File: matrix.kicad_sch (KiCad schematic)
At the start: 138 parts, among them SW1 SW_Push, SW10 SW_Push, SW11 SW_Push, SW12 SW_Push, SW13 SW_Push, SW14 SW_Push, SW15 SW_Push, SW16 SW_Push, SW17 SW_Push, SW18 SW_Push, SW19 SW_Push, SW2 SW_Push, SW20 SW_Push, SW21 SW_Push, SW22 SW_Push, SW23 SW_Push, SW24 SW_Push, SW25 SW_Push, SW26 SW_Push, SW27 SW_Push, SW28 SW_Push, SW29 SW_Push, SW3 SW_Push, SW30 SW_Push, SW31 SW_Push, SW32 SW_Push, SW33 SW_Push, SW34 SW_Push, SW35 SW_Push, SW36 SW_Push, SW37 SW_Push, SW38 SW_Push, SW39 SW_Push, SW4 SW_Push, SW40 SW_Push, SW41 SW_Push, SW42 SW_Push, SW43 SW_Push, SW44 SW_Push, SW45 SW_Push, SW46 SW_Push, SW47 SW_Push, SW48 SW_Push, SW49 SW_Push, SW5 SW_Push, SW50 SW_Push, SW51 SW_Push, SW52 SW_Push, SW53 SW_Push, SW54 SW_Push, SW55 SW_Push, SW56 SW_Push, SW57 SW_Push, SW58 SW_Push, SW59 SW_Push, SW6 SW_Push, SW60 SW_Push, SW61 SW_Push, SW62 SW_Push, SW63 SW_Push, SW65 SW_Push, SW66 SW_Push, SW67 SW_Push, SW69 SW_Push, SW7 SW_Push, SW70 SW_Push, SW71 SW_Push, SW8 SW_Push, SW9 SW_Push

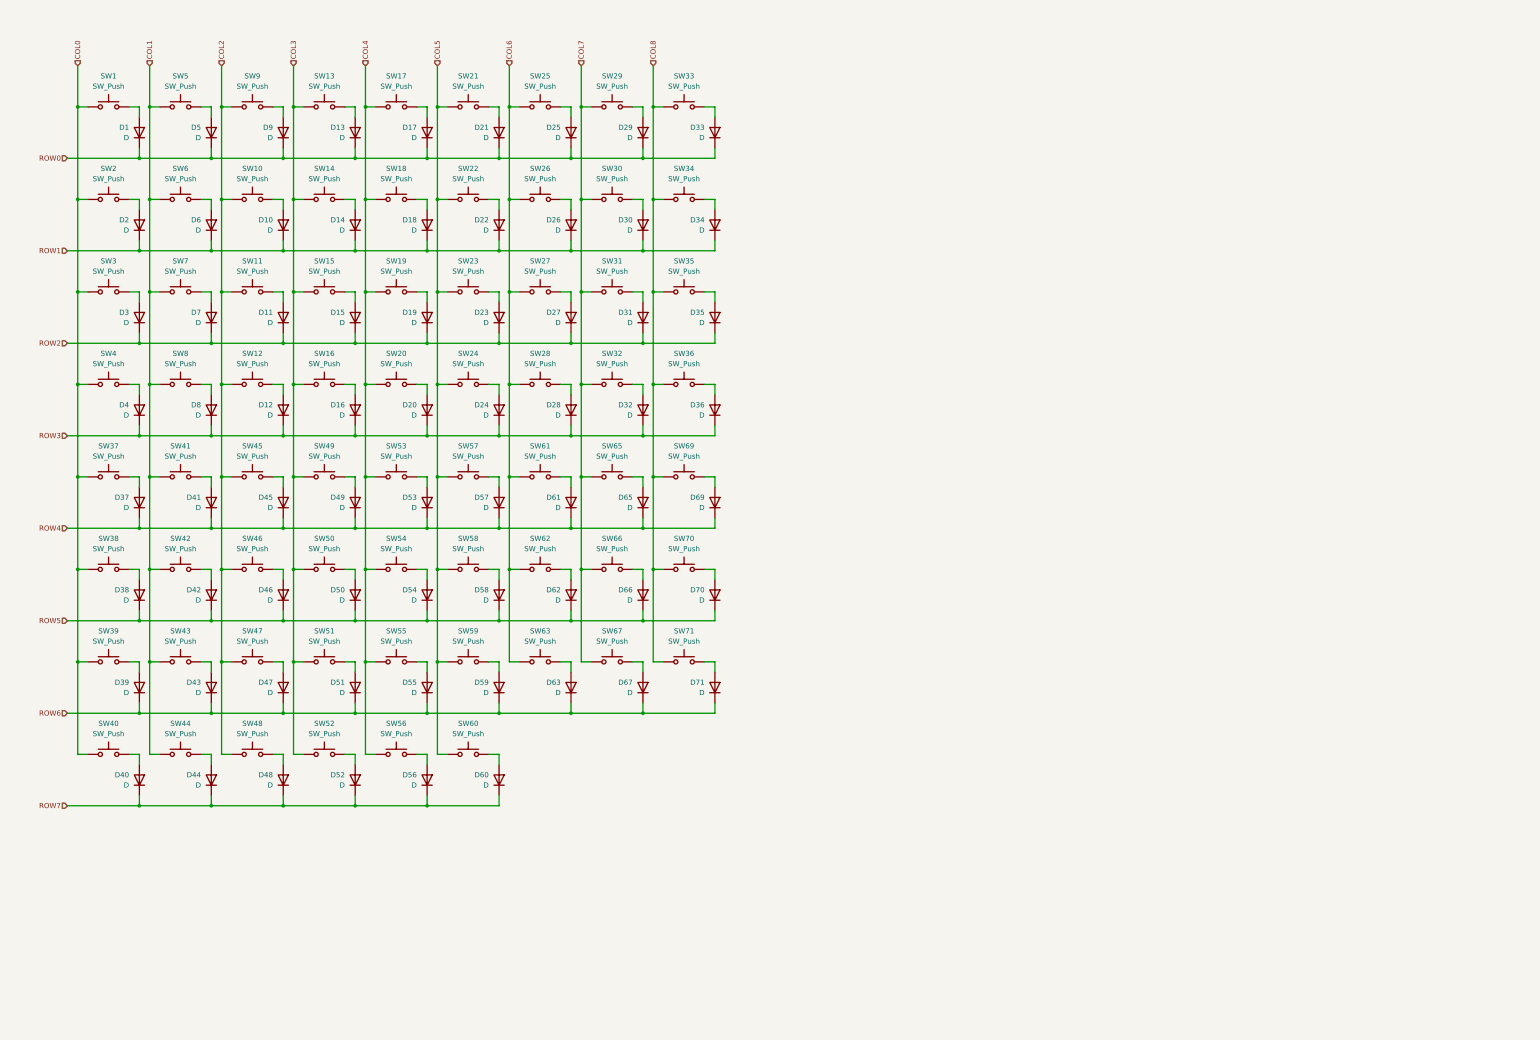
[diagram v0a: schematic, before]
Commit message: update layout and switch to wired
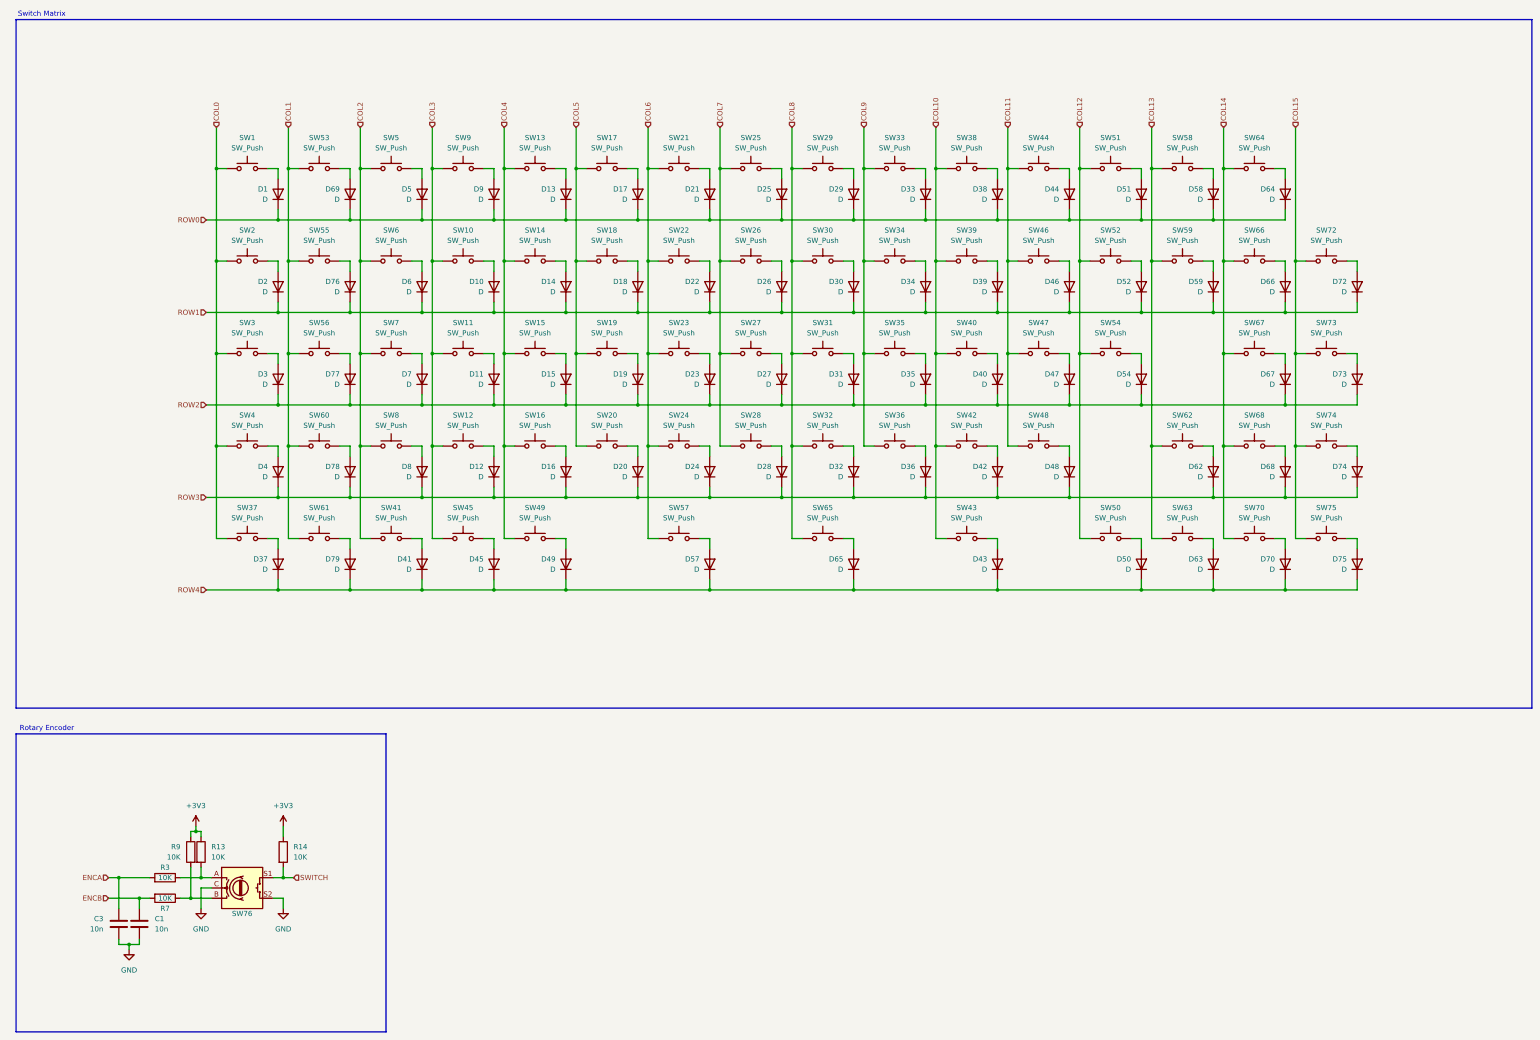
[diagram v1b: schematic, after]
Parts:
- removed D53, D55, D56, D60, D61, D71: D, symbol Device:D
- removed SW69, SW71: SW_Push, symbol Switch:SW_Push
- added C1, C3: 10n, symbol Device:C
- added D64, D68, D72, D73, D74, D75, D76, D77, D78, D79: D, symbol Device:D
- added R13, R14, R3, R7, R9: 10K, symbol Device:R
- added SW64, SW68, SW72, SW73, SW74, SW75: SW_Push, symbol Switch:SW_Push
- added SW76: RotaryEncoder_Switch, symbol Device:RotaryEncoder_Switch
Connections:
- net COL0: no longer SW38.1, SW39.1, SW40.1
- net COL1: now also SW53.1, SW55.1, SW56.1, SW60.1, SW61.1; no longer SW41.1, SW42.1, SW43.1, SW44.1, SW5.1, SW6.1, SW7.1, SW8.1
- net COL2: now also SW41.1, SW5.1, SW6.1, SW7.1, SW8.1; no longer SW10.1, SW11.1, SW12.1, SW45.1, SW46.1, SW47.1, SW48.1, SW9.1
- net COL3: now also SW10.1, SW11.1, SW12.1, SW45.1, SW9.1; no longer SW13.1, SW14.1, SW15.1, SW16.1, SW49.1, SW50.1, SW51.1, SW52.1
- net COL4: now also SW13.1, SW14.1, SW15.1, SW16.1, SW49.1; no longer SW17.1, SW18.1, SW19.1, SW20.1, SW53.1, SW54.1, SW55.1, SW56.1
- net COL5: now also SW17.1, SW18.1, SW19.1, SW20.1; no longer SW21.1, SW22.1, SW23.1, SW24.1, SW57.1, SW58.1, SW59.1, SW60.1
- net COL6: now also SW21.1, SW22.1, SW23.1, SW24.1, SW57.1; no longer SW25.1, SW26.1, SW27.1, SW28.1, SW61.1, SW62.1, SW63.1
- net COL7: now also SW25.1, SW26.1, SW27.1, SW28.1; no longer SW29.1, SW30.1, SW31.1, SW32.1, SW65.1, SW66.1, SW67.1
- net COL8: now also SW29.1, SW30.1, SW31.1, SW32.1, SW65.1; no longer SW33.1, SW34.1, SW35.1, SW36.1, SW70.1
- net ROW0: now also D38.1 (K), D44.1 (K), D51.1 (K), D58.1 (K), D69.1 (K), D64.1 (K)
- net ROW1: now also D39.1 (K), D46.1 (K), D52.1 (K), D59.1 (K), D66.1 (K), D72.1 (K), D76.1 (K)
- net ROW2: now also D40.1 (K), D47.1 (K), D54.1 (K), D67.1 (K), D73.1 (K), D77.1 (K)
- net ROW3: now also D42.1 (K), D48.1 (K), D62.1 (K), D68.1 (K), D74.1 (K), D78.1 (K)
- net ROW4: now also D43.1 (K), D50.1 (K), D63.1 (K), D70.1 (K), D75.1 (K), D79.1 (K); no longer D69.1 (K)
- net at SW55.2: now also D76.2 (A)
- net at SW60.2: now also D78.2 (A)
- net at SW61.2: now also D79.2 (A)
- net at SW56.2: now also D77.2 (A)
- net at SW53.2: now also D69.2 (A)
- removed net ROW5: D38.1 (K), D42.1 (K), D46.1 (K), D50.1 (K), D54.1 (K), D58.1 (K), D62.1 (K), D66.1 (K), D70.1 (K)
- removed net ROW6: D39.1 (K), D43.1 (K), D47.1 (K), D51.1 (K), D59.1 (K), D63.1 (K), D67.1 (K)
- removed net ROW7: D40.1 (K), D44.1 (K), D48.1 (K), D52.1 (K)
- new net: D74.2 (A), SW74.2
- new net: R13.2, R3.1, SW76.A
- new net: D75.2 (A), SW75.2
- new net: D68.2 (A), SW68.2
- new net: D72.2 (A), SW72.2
- new net: D73.2 (A), SW73.2
- new net: R7.1, R9.2, SW76.B
- new net: D64.2 (A), SW64.2
- new net +3V3: R13.1, R14.1, R9.1
- new net COL10: SW38.1, SW39.1, SW40.1, SW42.1, SW43.1
- new net COL11: SW44.1, SW46.1, SW47.1, SW48.1
- new net COL12: SW50.1, SW51.1, SW52.1, SW54.1
- new net COL13: SW58.1, SW59.1, SW62.1, SW63.1
- new net COL14: SW64.1, SW66.1, SW67.1, SW68.1, SW70.1
- new net COL15: SW72.1, SW73.1, SW74.1, SW75.1
- new net COL9: SW33.1, SW34.1, SW35.1, SW36.1
- new net ENCA: C3.1, R3.2
- new net ENCB: C1.1, R7.2
- new net GND: C1.2, C3.2, SW76.C, SW76.S2
- new net SWITCH: R14.2, SW76.S1
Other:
- note added: "Rotary Encoder"
- note added: "Switch Matrix"
- moved on the sheet: D10, D11, D12, D13, D14, D15, D16, D17, D18, D19, D20, D21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

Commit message: work on layout and routing
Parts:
- C14: renamed from C3; footprint (none) -> Capacitor_SMD:C_0402_1005Metric
- C15: renamed from C1; footprint (none) -> Capacitor_SMD:C_0402_1005Metric
- D1, D22: footprint (none) -> Diode_SMD:D_SOD-123
- D10: renamed from D33; footprint (none) -> Diode_SMD:D_SOD-123
- D11: renamed from D38; footprint (none) -> Diode_SMD:D_SOD-123
- D12: renamed from D44; footprint (none) -> Diode_SMD:D_SOD-123
- D13: renamed from D51; footprint (none) -> Diode_SMD:D_SOD-123
- D14: renamed from D58; footprint (none) -> Diode_SMD:D_SOD-123
- D15: renamed from D64; footprint (none) -> Diode_SMD:D_SOD-123
- D16: renamed from D2; footprint (none) -> Diode_SMD:D_SOD-123
- D17: renamed from D76; footprint (none) -> Diode_SMD:D_SOD-123
- D18: renamed from D6; footprint (none) -> Diode_SMD:D_SOD-123
- D19: renamed from D10; footprint (none) -> Diode_SMD:D_SOD-123
- D2: renamed from D69; footprint (none) -> Diode_SMD:D_SOD-123
- D20: renamed from D14; footprint (none) -> Diode_SMD:D_SOD-123
- D21: renamed from D18; footprint (none) -> Diode_SMD:D_SOD-123
- D23: renamed from D26; footprint (none) -> Diode_SMD:D_SOD-123
- D24: renamed from D30; footprint (none) -> Diode_SMD:D_SOD-123
- D25: renamed from D34; footprint (none) -> Diode_SMD:D_SOD-123
- D26: renamed from D39; footprint (none) -> Diode_SMD:D_SOD-123
- D27: renamed from D46; footprint (none) -> Diode_SMD:D_SOD-123
- D28: renamed from D52; footprint (none) -> Diode_SMD:D_SOD-123
- D29: renamed from D59; footprint (none) -> Diode_SMD:D_SOD-123
- D3: renamed from D5; footprint (none) -> Diode_SMD:D_SOD-123
- D30: renamed from D66; footprint (none) -> Diode_SMD:D_SOD-123
- D31: renamed from D72; footprint (none) -> Diode_SMD:D_SOD-123
- D32: renamed from D3; footprint (none) -> Diode_SMD:D_SOD-123
- D33: renamed from D77; footprint (none) -> Diode_SMD:D_SOD-123
- D34: renamed from D7; footprint (none) -> Diode_SMD:D_SOD-123
- D35: renamed from D11; footprint (none) -> Diode_SMD:D_SOD-123
- D36: renamed from D15; footprint (none) -> Diode_SMD:D_SOD-123
- D37: renamed from D19; footprint (none) -> Diode_SMD:D_SOD-123
- D38: renamed from D23; footprint (none) -> Diode_SMD:D_SOD-123
- D39: renamed from D27; footprint (none) -> Diode_SMD:D_SOD-123
- D4: renamed from D9; footprint (none) -> Diode_SMD:D_SOD-123
- D40: renamed from D31; footprint (none) -> Diode_SMD:D_SOD-123
- D41: renamed from D35; footprint (none) -> Diode_SMD:D_SOD-123
- D42: renamed from D40; footprint (none) -> Diode_SMD:D_SOD-123
- D43: renamed from D47; footprint (none) -> Diode_SMD:D_SOD-123
- D44: renamed from D54; footprint (none) -> Diode_SMD:D_SOD-123
- D45: renamed from D67; footprint (none) -> Diode_SMD:D_SOD-123
- D46: renamed from D73; footprint (none) -> Diode_SMD:D_SOD-123
- D47: renamed from D4; footprint (none) -> Diode_SMD:D_SOD-123
- D48: renamed from D78; footprint (none) -> Diode_SMD:D_SOD-123
- D49: renamed from D8; footprint (none) -> Diode_SMD:D_SOD-123
- D5: renamed from D13; footprint (none) -> Diode_SMD:D_SOD-123
- D50: renamed from D12; footprint (none) -> Diode_SMD:D_SOD-123
- D51: renamed from D16; footprint (none) -> Diode_SMD:D_SOD-123
- D52: renamed from D20; footprint (none) -> Diode_SMD:D_SOD-123
- D53: renamed from D24; footprint (none) -> Diode_SMD:D_SOD-123
- D54: renamed from D28; footprint (none) -> Diode_SMD:D_SOD-123
- D55: renamed from D32; footprint (none) -> Diode_SMD:D_SOD-123
- D56: renamed from D36; footprint (none) -> Diode_SMD:D_SOD-123
- D57: renamed from D42; footprint (none) -> Diode_SMD:D_SOD-123
- D58: renamed from D48; footprint (none) -> Diode_SMD:D_SOD-123
- D59: renamed from D62; footprint (none) -> Diode_SMD:D_SOD-123
- D6: renamed from D17; footprint (none) -> Diode_SMD:D_SOD-123
- D60: renamed from D68; footprint (none) -> Diode_SMD:D_SOD-123
- D61: renamed from D74; footprint (none) -> Diode_SMD:D_SOD-123
- D62: renamed from D37; footprint (none) -> Diode_SMD:D_SOD-123
- D63: renamed from D79; footprint (none) -> Diode_SMD:D_SOD-123
- D64: renamed from D41; footprint (none) -> Diode_SMD:D_SOD-123
- D65: renamed from D45; footprint (none) -> Diode_SMD:D_SOD-123
- D66: renamed from D49; footprint (none) -> Diode_SMD:D_SOD-123
- D67: renamed from D57; footprint (none) -> Diode_SMD:D_SOD-123
- D68: renamed from D65; footprint (none) -> Diode_SMD:D_SOD-123
- D69: renamed from D43; footprint (none) -> Diode_SMD:D_SOD-123
- D7: renamed from D21; footprint (none) -> Diode_SMD:D_SOD-123
- D70: renamed from D50; footprint (none) -> Diode_SMD:D_SOD-123
- D71: renamed from D63; footprint (none) -> Diode_SMD:D_SOD-123
- D72: renamed from D70; footprint (none) -> Diode_SMD:D_SOD-123
- D73: renamed from D75; footprint (none) -> Diode_SMD:D_SOD-123
- D8: renamed from D25; footprint (none) -> Diode_SMD:D_SOD-123
- D9: renamed from D29; footprint (none) -> Diode_SMD:D_SOD-123
- R12: renamed from R9; footprint (none) -> Resistor_SMD:R_0402_1005Metric
- R13, R14: footprint (none) -> Resistor_SMD:R_0402_1005Metric
- R15: renamed from R3; footprint (none) -> Resistor_SMD:R_0402_1005Metric
- R16: renamed from R7; footprint (none) -> Resistor_SMD:R_0402_1005Metric
- SW1, SW22: footprint (none) -> PCM_marbastlib-mx:SW_MX_1u
- SW10: renamed from SW33; footprint (none) -> PCM_marbastlib-mx:SW_MX_1u
- SW11: renamed from SW38; footprint (none) -> PCM_marbastlib-mx:SW_MX_1u
- SW12: renamed from SW44; footprint (none) -> PCM_marbastlib-mx:SW_MX_1u
- SW13: renamed from SW51; footprint (none) -> PCM_marbastlib-mx:SW_MX_1u
- SW14: renamed from SW58; footprint (none) -> PCM_marbastlib-mx:SW_MX_1u
- SW15: renamed from SW64; footprint (none) -> PCM_marbastlib-mx:SW_MX_1u
- SW16: renamed from SW2; footprint (none) -> PCM_marbastlib-mx:SW_MX_1u
- SW17: renamed from SW55; footprint (none) -> PCM_marbastlib-mx:SW_MX_1u
- SW18: renamed from SW6; footprint (none) -> PCM_marbastlib-mx:SW_MX_1u
- SW19: renamed from SW10; footprint (none) -> PCM_marbastlib-mx:SW_MX_1u
- SW2: renamed from SW53; footprint (none) -> PCM_marbastlib-mx:SW_MX_1u
- SW20: renamed from SW14; footprint (none) -> PCM_marbastlib-mx:SW_MX_1u
- SW21: renamed from SW18; footprint (none) -> PCM_marbastlib-mx:SW_MX_1u
- SW23: renamed from SW26; footprint (none) -> PCM_marbastlib-mx:SW_MX_1u
- SW24: renamed from SW30; footprint (none) -> PCM_marbastlib-mx:SW_MX_1u
- SW25: renamed from SW34; footprint (none) -> PCM_marbastlib-mx:SW_MX_1u
- SW26: renamed from SW39; footprint (none) -> PCM_marbastlib-mx:SW_MX_1u
- SW27: renamed from SW46; footprint (none) -> PCM_marbastlib-mx:SW_MX_1u
- SW28: renamed from SW52; footprint (none) -> PCM_marbastlib-mx:SW_MX_1u
- SW29: renamed from SW59; footprint (none) -> PCM_marbastlib-mx:SW_MX_1u
- SW3: renamed from SW5; footprint (none) -> PCM_marbastlib-mx:SW_MX_1u
- SW30: renamed from SW66; footprint (none) -> PCM_marbastlib-mx:SW_MX_1u
- SW31: renamed from SW72; footprint (none) -> PCM_marbastlib-mx:SW_MX_1u
- SW32: renamed from SW3; footprint (none) -> PCM_marbastlib-mx:SW_MX_1u
- SW33: renamed from SW56; footprint (none) -> PCM_marbastlib-mx:SW_MX_1u
- SW34: renamed from SW7; footprint (none) -> PCM_marbastlib-mx:SW_MX_1u
- SW35: renamed from SW11; footprint (none) -> PCM_marbastlib-mx:SW_MX_1u
- SW36: renamed from SW15; footprint (none) -> PCM_marbastlib-mx:SW_MX_1u
- SW37: renamed from SW19; footprint (none) -> PCM_marbastlib-mx:SW_MX_1u
- SW38: renamed from SW23; footprint (none) -> PCM_marbastlib-mx:SW_MX_1u
- SW39: renamed from SW27; footprint (none) -> PCM_marbastlib-mx:SW_MX_1u
- SW4: renamed from SW9; footprint (none) -> PCM_marbastlib-mx:SW_MX_1u
- SW40: renamed from SW31; footprint (none) -> PCM_marbastlib-mx:SW_MX_1u
- SW41: renamed from SW35; footprint (none) -> PCM_marbastlib-mx:SW_MX_1u
- SW42: renamed from SW40; footprint (none) -> PCM_marbastlib-mx:SW_MX_1u
- SW43: renamed from SW47; footprint (none) -> PCM_marbastlib-mx:SW_MX_1u
- SW44: renamed from SW54; footprint (none) -> PCM_marbastlib-mx:SW_MX_1u
- SW45: renamed from SW67; footprint (none) -> PCM_marbastlib-mx:SW_MX_1u
- SW46: renamed from SW73; footprint (none) -> PCM_marbastlib-mx:SW_MX_1u
- SW47: renamed from SW4; footprint (none) -> PCM_marbastlib-mx:SW_MX_1u
- SW48: renamed from SW60; footprint (none) -> PCM_marbastlib-mx:SW_MX_1u
- SW49: renamed from SW8; footprint (none) -> PCM_marbastlib-mx:SW_MX_1u
- SW5: renamed from SW13; footprint (none) -> PCM_marbastlib-mx:SW_MX_1u
- SW50: renamed from SW12; footprint (none) -> PCM_marbastlib-mx:SW_MX_1u
- SW51: renamed from SW16; footprint (none) -> PCM_marbastlib-mx:SW_MX_1u
- SW52: renamed from SW20; footprint (none) -> PCM_marbastlib-mx:SW_MX_1u
- SW53: renamed from SW24; footprint (none) -> PCM_marbastlib-mx:SW_MX_1u
- SW54: renamed from SW28; footprint (none) -> PCM_marbastlib-mx:SW_MX_1u
- SW55: renamed from SW32; footprint (none) -> PCM_marbastlib-mx:SW_MX_1u
- SW56: renamed from SW36; footprint (none) -> PCM_marbastlib-mx:SW_MX_1u
- SW57: renamed from SW42; footprint (none) -> PCM_marbastlib-mx:SW_MX_1u
- SW58: renamed from SW48; footprint (none) -> PCM_marbastlib-mx:SW_MX_1u
- SW59: renamed from SW62; footprint (none) -> PCM_marbastlib-mx:SW_MX_1u
- SW6: renamed from SW17; footprint (none) -> PCM_marbastlib-mx:SW_MX_1u
- SW60: renamed from SW68; footprint (none) -> PCM_marbastlib-mx:SW_MX_1u
- SW61: renamed from SW74; footprint (none) -> PCM_marbastlib-mx:SW_MX_1u
- SW62: renamed from SW37; footprint (none) -> PCM_marbastlib-mx:SW_MX_1u
- SW63: renamed from SW61; footprint (none) -> PCM_marbastlib-mx:SW_MX_1u
- SW64: renamed from SW41; footprint (none) -> PCM_marbastlib-mx:SW_MX_1u
- SW65: renamed from SW45; footprint (none) -> PCM_marbastlib-mx:SW_MX_1u
- SW66: renamed from SW49; footprint (none) -> PCM_marbastlib-mx:SW_MX_1u
- SW67: renamed from SW57; footprint (none) -> PCM_marbastlib-mx:SW_MX_1u
- SW68: renamed from SW65; footprint (none) -> PCM_marbastlib-mx:SW_MX_1u
- SW69: renamed from SW43; footprint (none) -> PCM_marbastlib-mx:SW_MX_1u
- SW7: renamed from SW21; footprint (none) -> PCM_marbastlib-mx:SW_MX_1u
- SW70: renamed from SW50; footprint (none) -> PCM_marbastlib-mx:SW_MX_1u
- SW71: renamed from SW63; footprint (none) -> PCM_marbastlib-mx:SW_MX_1u
- SW72: renamed from SW70; footprint (none) -> PCM_marbastlib-mx:SW_MX_1u
- SW73: renamed from SW75; footprint (none) -> PCM_marbastlib-mx:SW_MX_1u
- SW76: footprint (none) -> PCM_marbastlib-various:ROT_Alps_EC11E-Switch
- SW8: renamed from SW25; footprint (none) -> PCM_marbastlib-mx:SW_MX_1u
- SW9: renamed from SW29; footprint (none) -> PCM_marbastlib-mx:SW_MX_1u

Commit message: backup before encoder fix
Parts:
- added C16: 10n, Capacitor_SMD:C_0603_1608Metric, symbol Device:C
- added D76: D, Diode_SMD:D_SOD-123, symbol Device:D
- added R3: 10K, Resistor_SMD:R_0603_1608Metric, symbol Device:R
- added SW77: SW_Push, PCM_marbastlib-mx:SW_MX_1u, symbol Switch:SW_Push
- C14: footprint Capacitor_SMD:C_0402_1005Metric -> Capacitor_SMD:C_0603_1608Metric; LCSC (none) -> C907967
- C15: footprint Capacitor_SMD:C_0402_1005Metric -> Capacitor_SMD:C_0603_1608Metric; LCSC (none) -> C466231
- R12: footprint Resistor_SMD:R_0402_1005Metric -> Resistor_SMD:R_0603_1608Metric; LCSC (none) -> C25930
- R13, R14, R15, R16: footprint Resistor_SMD:R_0402_1005Metric -> Resistor_SMD:R_0603_1608Metric
- SW17, SW30, SW69, SW70: footprint PCM_marbastlib-mx:SW_MX_1u -> PCM_marbastlib-mx:SW_MX_1.5u; now left out of the parts list
- SW33, SW59, SW67: footprint PCM_marbastlib-mx:SW_MX_1u -> PCM_marbastlib-mx:SW_MX_1.75u; now left out of the parts list
- SW63, SW64, SW65: footprint PCM_marbastlib-mx:SW_MX_1u -> PCM_marbastlib-mx:SW_MX_1.25u; now left out of the parts list
- SW76: symbol Device:RotaryEncoder_Switch -> Device:RotaryEncoder_Switch_MP
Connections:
- net COL15: now also SW77.1
- net GND: now also SW76.MP, C16.2
- net ROW0: now also D76.1 (K)
- net SWITCH: now also C16.1, R3.1; no longer R14.2, SW76.S1
- new net: D76.2 (A), SW77.2
- new net: R14.2, R3.2, SW76.S1
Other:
- moved on the sheet: C14, C15, R12, R13, R14, R15, R16
